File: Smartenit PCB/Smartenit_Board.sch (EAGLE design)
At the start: 86 parts, among them J1 2X5CONNECTOR1.27MM, Q1 QUARTZ_3.58M_2PIN, U1 SN74LVC1G3157, U2 ADE7953, U3 ESP-WROOM-32

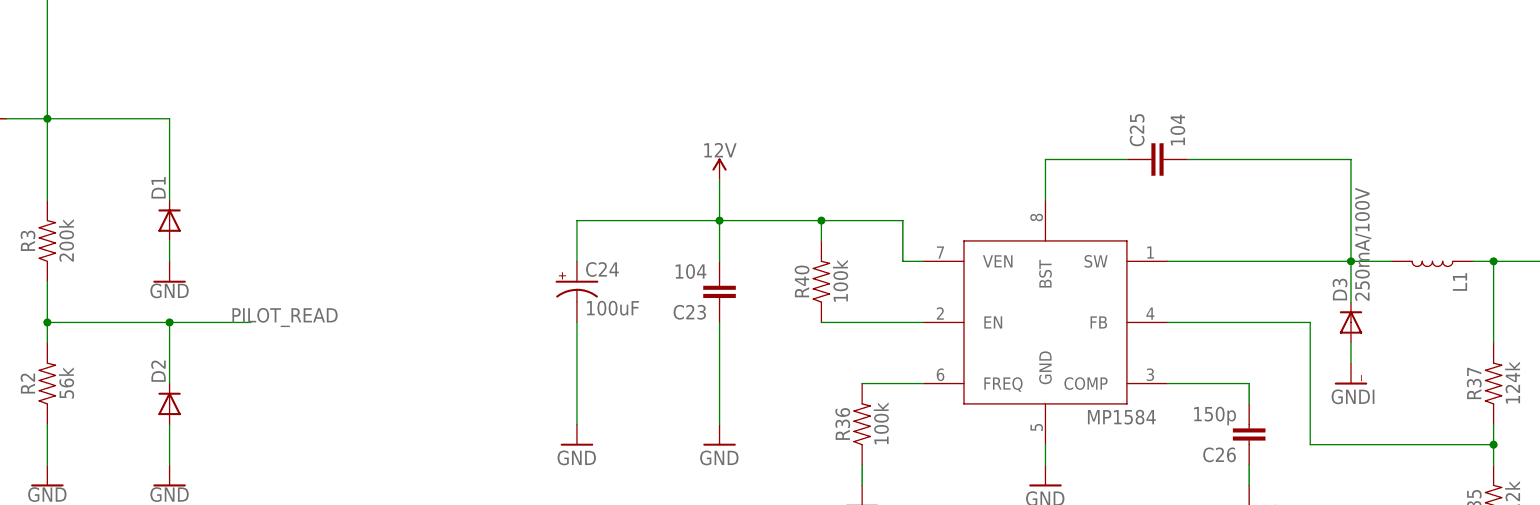
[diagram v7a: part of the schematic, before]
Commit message: fixed diodes
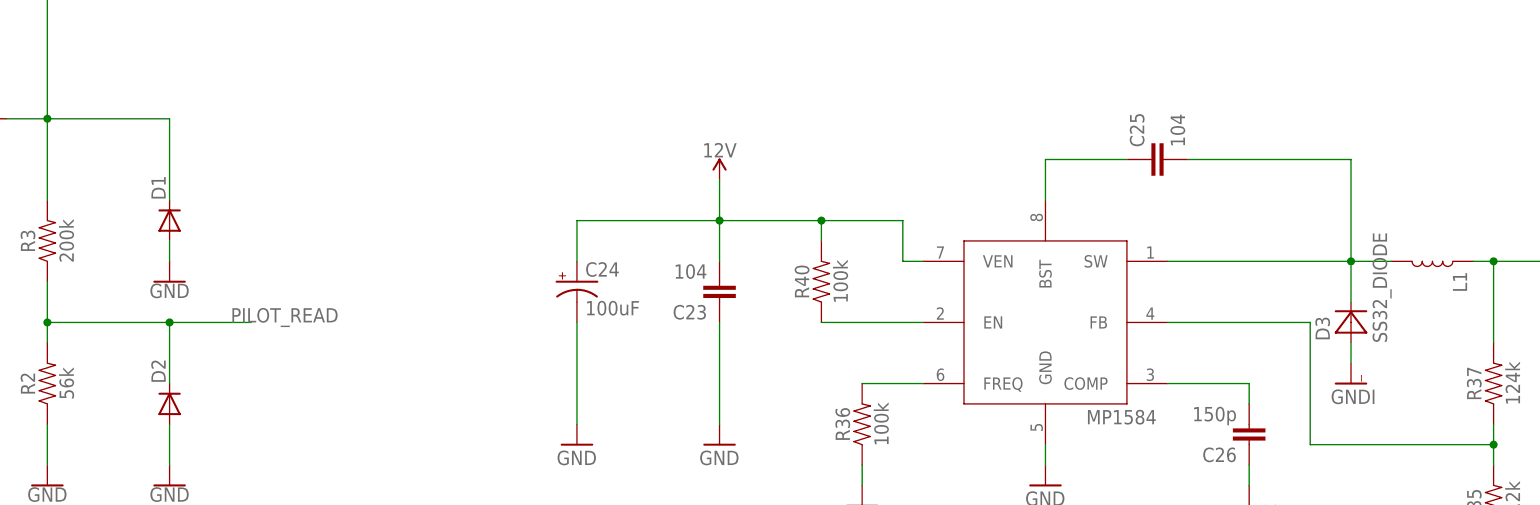
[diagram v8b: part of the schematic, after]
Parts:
- D1: value (none) -> P6SMB16A; device SparkFun:DIODESMA -> diode:DIODE-SMB
- D3: value 250mA/100V -> SS32_DIODE; device diode:DIODE-DO214BA -> Smart_Charger:SS32_DIODE
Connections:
- net AGND: now also D3.P; no longer D3.A
- net N$18: now also D3.N; no longer D3.C
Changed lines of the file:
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@@
 <part name="GNDI6" library="SparkFun" deviceset="GND" device=""/>
 <part name="GNDI7" library="SparkFun" deviceset="GND" device=""/>
-<part name="D3" library="diode" library_urn="urn:adsk.eagle:library:210" deviceset="DIODE-" device="DO214BA" package3d_urn="urn:adsk.eagle:package:43453/2" value="250mA/100V"/>
 <part name="GNDI8" library="supply1" deviceset="GNDI" device=""/>
 <part name="GNDI9" library="SparkFun" deviceset="GND" device=""/>
@@
 <part name="GND3" library="SparkFun-PowerSymbols" deviceset="GND" device=""/>
 <part name="D2" library="SparkFun" deviceset="DIODE" device="SOD"/>
-<part name="D1" library="SparkFun" deviceset="DIODE" device="SMA"/>
 <part name="GND4" library="SparkFun-PowerSymbols" deviceset="GND" device=""/>
 <part name="GND5" library="SparkFun-PowerSymbols" deviceset="GND" device=""/>
@@
 <part name="GNDI29" library="SparkFun" deviceset="GND" device=""/>
 <part name="GNDI30" library="SparkFun" deviceset="GND" device=""/>
+<part name="D3" library="Smart_Charger" deviceset="SS32_DIODE" device=""/>
+<part name="D1" library="diode" library_urn="urn:adsk.eagle:library:210" deviceset="DIODE-" device="SMB" package3d_urn="urn:adsk.eagle:package:43404/2" value="P6SMB16A"/>
 </parts>
 <sheets>
@@
 <instance part="GNDI6" gate="1" x="-86.36" y="119.38"/>
 <instance part="GNDI7" gate="1" x="-152.4" y="139.7"/>
-<instance part="D3" gate="G$1" x="-73.66" y="154.94" rot="R90"/>
 <instance part="GNDI8" gate="G$1" x="-73.66" y="147.32"/>
 <instance part="GNDI9" gate="1" x="-55.88" y="119.38"/>
@@
 <instance part="GND3" gate="1" x="-236.22" y="134.62"/>
 <instance part="D2" gate="G$1" x="-220.98" y="144.78" rot="R90"/>
-<instance part="D1" gate="G$1" x="-220.98" y="167.64" rot="R90"/>
 <instance part="GND4" gate="1" x="-220.98" y="134.62"/>
 <instance part="GND5" gate="1" x="-220.98" y="160.02"/>
@@
 <instance part="GNDI29" gate="1" x="10.16" y="2.54"/>
 <instance part="GNDI30" gate="1" x="-205.74" y="-93.98"/>
+<instance part="D3" gate="G$1" x="-73.66" y="154.94" rot="R90"/>
+<instance part="D1" gate="G$1" x="-220.98" y="167.64" smashed="yes" rot="R90">
+<attribute name="NAME" x="-221.4626" y="170.18" size="1.778" layer="95" rot="R90"/>
+</instance>
 </instances>
 <busses>
@@
 <segment>
 <pinref part="U$4" gate="G$1" pin="SW"/>
-<pinref part="D3" gate="G$1" pin="C"/>
 <wire x1="-96.52" y1="162.56" x2="-73.66" y2="162.56" width="0.1524" layer="91"/>
 <wire x1="-73.66" y1="162.56" x2="-73.66" y2="157.48" width="0.1524" layer="91"/>
@@
 <wire x1="-93.98" y1="175.26" x2="-73.66" y2="175.26" width="0.1524" layer="91"/>
 <wire x1="-73.66" y1="175.26" x2="-73.66" y2="162.56" width="0.1524" layer="91"/>
+<pinref part="D3" gate="G$1" pin="N"/>
 </segment>
 </net>
@@
 <wire x1="-236.22" y1="180.34" x2="-220.98" y2="180.34" width="0.1524" layer="91"/>
 <junction x="-236.22" y="180.34"/>
-<pinref part="D1" gate="G$1" pin="C"/>
 <wire x1="-220.98" y1="180.34" x2="-220.98" y2="170.18" width="0.1524" layer="91"/>
 <wire x1="-236.22" y1="180.34" x2="-236.22" y2="203.2" width="0.1524" layer="91"/>
 <wire x1="-236.22" y1="203.2" x2="-226.06" y2="203.2" width="0.1524" layer="91"/>
 <label x="-231.14" y="203.2" size="1.778" layer="95"/>
+<pinref part="D1" gate="G$1" pin="C"/>
 </segment>
 </net>
@@
 <segment>
 <pinref part="GNDI8" gate="G$1" pin="GNDI"/>
-<pinref part="D3" gate="G$1" pin="A"/>
 <wire x1="-73.66" y1="149.86" x2="-73.66" y2="152.4" width="0.1524" layer="91"/>
+<pinref part="D3" gate="G$1" pin="P"/>
 </segment>
 <segment>
@@
 <segment>
 <pinref part="GND5" gate="1" pin="GND"/>
+<wire x1="-220.98" y1="162.56" x2="-220.98" y2="165.1" width="0.1524" layer="91"/>
 <pinref part="D1" gate="G$1" pin="A"/>
-<wire x1="-220.98" y1="162.56" x2="-220.98" y2="165.1" width="0.1524" layer="91"/>
-</segment>
-<segment>
+</segment>
+<segment>
